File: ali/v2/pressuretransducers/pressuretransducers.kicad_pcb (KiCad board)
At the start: 4 copper layers, 85 x 76 mm, 235 parts, among them J1 Conn_02x01, J10 Conn_01x02, J11 Conn_01x02, J12 Conn_01x02, J13 Conn_01x02, J14 Conn_01x02, J15 Conn_01x02, J16 Conn_01x02, J17 Conn_01x02, J18 Conn_01x02, J19 Conn_01x02, J2 Conn_01x05, J20 Conn_01x02, J21 Conn_01x02, J22 Conn_01x02, J23 Conn_01x02, J24 Conn_01x02, J25 Conn_01x02, J3 USB_C_Receptacle_USB2.0_16P, J4 Conn_01x15, J5 Conn_02x09_Counter_Clockwise, J6 Screw_Terminal_01x02, J7 Screw_Terminal_01x02, J8 Conn_01x03, J9 Vertical Ethernet, SW1 SKRPANE010, U1 STM32H563RIV6, U2 AP2112K-3.3, U3 TJA1462ATK, U4 LAN8742AI, U5 ADS131M08IRSN, U6 ADS131M08IRSN, Y1 25 MHz, Y2 8.192 MHz, Y3 25 MHz

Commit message: Minor thermocouple updates
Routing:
- net /Connectivity/ETH_MDIO: track 26.1 -> 26.8 mm
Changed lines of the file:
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@@
+	)
+	(segment
+		(start 140.2625 120.375)
+		(end 140.2125 120.425)
+		(width 0.3)
+		(layer "B.Cu")
+		(net "/Connectivity/ETH_MDIO")
+	)
+	(segment
+		(start 140.2625 119.725)
+		(end 140.2625 120.375)
+		(width 0.3)
+		(layer "B.Cu")
+		(net "/Connectivity/ETH_MDIO")
 	)
 	(segment
@@
 	)
 	(segment
+		(start 131.1725 129.865)
+		(end 131.1725 132.925)
+		(width 0.15)
+		(layer "B.Cu")
+		(net "/Microcontroller/PB0")
+	)
+	(segment
+		(start 136.5125 108.425)
+		(end 133.6125 111.325)
+		(width 0.15)
+		(layer "B.Cu")
+		(net "/Microcontroller/PB0")
+	)
+	(segment
 		(start 145.8125 108.425)
 		(end 136.5125 108.425)
@@
 	)
 	(segment
-		(start 131.1725 128.865)
-		(end 131.1725 132.925)
-		(width 0.15)
-		(layer "B.Cu")
-		(net "/Microcontroller/PB0")
-	)
-	(segment
-		(start 133.6125 126.425)
-		(end 131.1725 128.865)
-		(width 0.15)
-		(layer "B.Cu")
-		(net "/Microcontroller/PB0")
-	)
-	(segment
-		(start 136.5125 108.425)
-		(end 133.6125 111.325)
+		(start 133.6125 127.425)
+		(end 131.1725 129.865)
 		(width 0.15)
 		(layer "B.Cu")
@@
 	(segment
 		(start 133.6125 111.325)
-		(end 133.6125 126.425)
-		(width 0.15)
-		(layer "B.Cu")
+		(end 133.6125 127.425)
+		(width 0.15)
+		(layer "B.Cu")

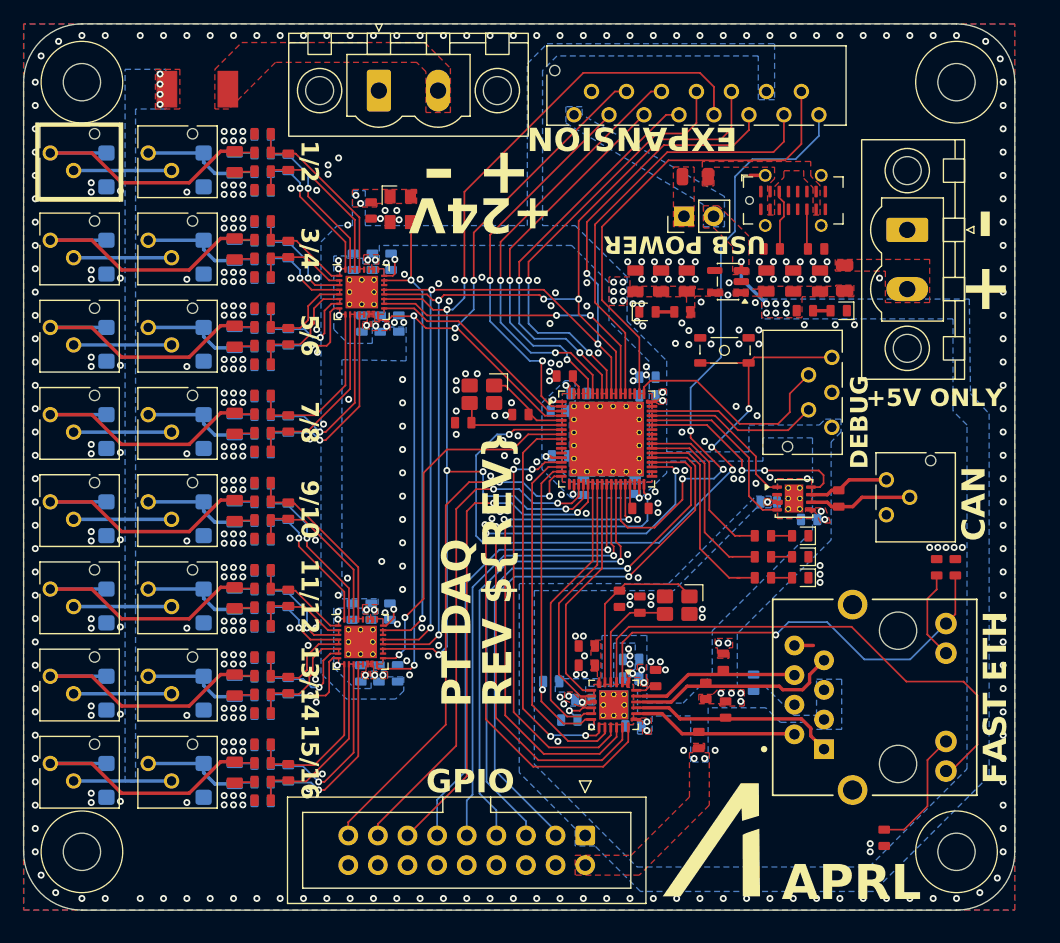
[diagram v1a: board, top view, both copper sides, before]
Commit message: Globally remove LCSC labels, update MPNs and IOCs, add +5V monitoring to DAQs, fix some footprints
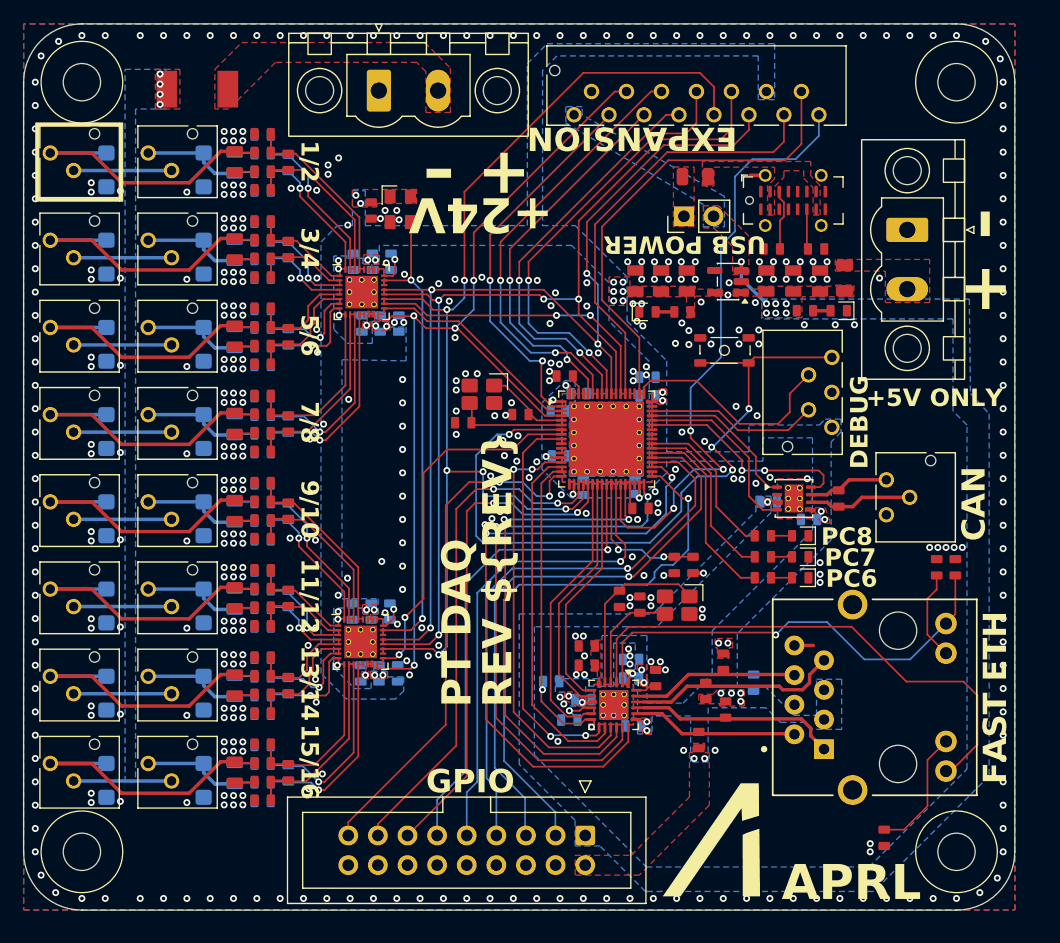
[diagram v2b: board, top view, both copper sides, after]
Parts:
- added R8: 10k, APRL_Passive:R_0603, F.Cu at (153.1, 109.7)
- added R9: 10k, APRL_Passive:R_0603, F.Cu at (151.5, 109.7)
- renumbered C18 to C12, C12 to C13, C13 to C14, C14 to C15, C15 to C16, C16 to C17, C17 to C18, J5 to J4, J4 to J5, R8 to R10, R9 to R11, R10 to R12, R11 to R13, R12 to R14, R13 to R15, R14 to R16, R15 to R17, R16 to R18, R17 to R19, R18 to R20, R19 to R21, R20 to R22, R21 to R23, R22 to R24, R23 to R25, R24 to R26, R25 to R27, R26 to R28, R27 to R29, R28 to R30, R29 to R31, R30 to R32, R31 to R33, R32 to R34, R33 to R35, R34 to R36, R35 to R37, R36 to R38, R37 to R39, R38 to R40, R39 to R41, R40 to R42, R41 to R43, R42 to R44, R43 to R45, R44 to R46, R45 to R47, R46 to R48, R47 to R49, R48 to R50, R49 to R51, R50 to R52, R51 to R53, R52 to R54, R53 to R55, R54 to R56, R55 to R57, R56 to R58, R57 to R59, R58 to R60, R59 to R61, R60 to R62, R61 to R63, R62 to R64, R63 to R65, R64 to R66, R65 to R67, R66 to R68
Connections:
- J4 pad 3: /Microcontroller/PD12 -> /Microcontroller/PB13
- J4 pad 5: /Microcontroller/PD11 -> /Microcontroller/PD12
- J4 pad 7: /Microcontroller/PB2 -> /Microcontroller/PD11
- J4 pad 9: /Microcontroller/PB1 -> /Microcontroller/PB2
- U1 pad 27: /Microcontroller/PB1 -> /Microcontroller/+5V_SENSE
- U1 pad 35: unconnected-(U1-PB13-Pad35) -> /Microcontroller/PB13
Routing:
- net /Microcontroller/PB13: track 0.00 -> 48.2 mm, vias 0 -> 1
- net /Microcontroller/PB1: track 40.9 -> 0.00 mm, vias 1 -> 0
- net /Microcontroller/+5V_SENSE: track 0.00 -> 12.6 mm, vias 0 -> 2
- net /Microcontroller/USER_LED_1: track 17.7 -> 16.7 mm
- net /Microcontroller/~{RST}: track 62.9 -> 63.8 mm
- net +5V: track 5.23 -> 6.13 mm, vias 8 -> 9
- net /Microcontroller/PD11: track 49.5 -> 48.7 mm
- net /Connectivity/ETH_TXD1: track 54.3 -> 53.5 mm
- net /Microcontroller/USER_LED_2: track 16.1 -> 15.3 mm
- net /Microcontroller/PD12: track 50.7 -> 50.0 mm
- net /Microcontroller/USER_LED_3: track 14.5 -> 13.8 mm
- net GND: vias 474 -> 475
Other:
- board text added: "PC6"
- board text added: "PC7"
- board text added: "PC8"
